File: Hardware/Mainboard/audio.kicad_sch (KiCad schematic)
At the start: 1 part, among them J8 Conn_02x08_Odd_Even

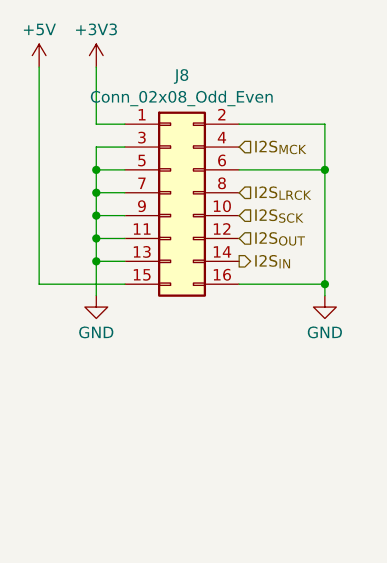
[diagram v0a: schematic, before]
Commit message: Adds more work on the mainboard schematic
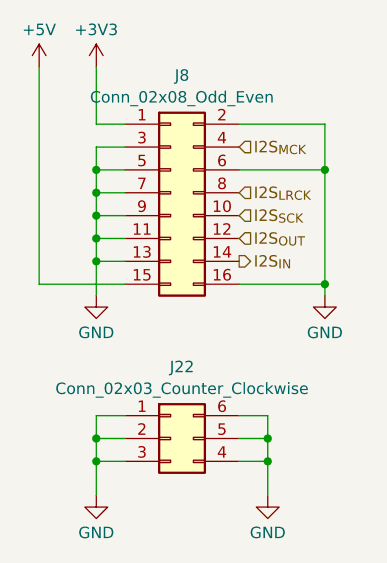
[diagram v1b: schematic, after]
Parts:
- added J22: Conn_02x03_Counter_Clockwise, Connector_PinSocket_2.54mm:PinSocket_2x03_P2.54mm_Vertical, symbol Connector_Generic:Conn_02x03_Counter_Clockwise
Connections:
- net GND: now also J22.1 (Pin_1), J22.2 (Pin_2), J22.3 (Pin_3), J22.4 (Pin_4), J22.5 (Pin_5), J22.6 (Pin_6)
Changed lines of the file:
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@@
   (junction (at 66.675 36.83) (diameter 0) (color 0 0 0 0)
   )
+  (junction (at 41.275 69.215) (diameter 0) (color 0 0 0 0)
+  )
   (junction (at 41.275 46.99) (diameter 0) (color 0 0 0 0)
   )
@@
   (junction (at 41.275 41.91) (diameter 0) (color 0 0 0 0)
   )
+  (junction (at 41.275 66.675) (diameter 0) (color 0 0 0 0)
+  )
   (junction (at 41.275 44.45) (diameter 0) (color 0 0 0 0)
   )
+  (junction (at 60.325 66.675) (diameter 0) (color 0 0 0 0)
+  )
   (junction (at 41.275 39.37) (diameter 0) (color 0 0 0 0)
   )
   (junction (at 66.675 49.53) (diameter 0) (color 0 0 0 0)
   )
+  (junction (at 60.325 69.215) (diameter 0) (color 0 0 0 0)
+  )
   (wire (pts (xy 66.675 36.83) (xy 66.675 49.53))
     (stroke (width 0) (type default))
   )
+  (wire (pts (xy 60.325 66.675) (xy 60.325 69.215))
+    (stroke (width 0) (type default))
+  )
   (wire (pts (xy 41.275 44.45) (xy 41.275 46.99))
     (stroke (width 0) (type default))
@@
     (stroke (width 0) (type default))
   )
+  (wire (pts (xy 41.275 69.215) (xy 41.275 73.025))
+    (stroke (width 0) (type default))
+  )
   (wire (pts (xy 66.675 49.53) (xy 66.675 50.8))
     (stroke (width 0) (type default))
   )
+  (wire (pts (xy 41.275 69.215) (xy 44.45 69.215))
+    (stroke (width 0) (type default))
+  )
+  (wire (pts (xy 60.325 69.215) (xy 60.325 73.025))
+    (stroke (width 0) (type default))
+  )
   (wire (pts (xy 41.275 25.4) (xy 41.275 31.75))
     (stroke (width 0) (type default))
   )
+  (wire (pts (xy 57.15 69.215) (xy 60.325 69.215))
+    (stroke (width 0) (type default))
+  )
+  (wire (pts (xy 44.45 64.135) (xy 41.275 64.135))
+    (stroke (width 0) (type default))
+  )
   (wire (pts (xy 41.275 36.83) (xy 41.275 39.37))
     (stroke (width 0) (type default))
   )
+  (wire (pts (xy 60.325 64.135) (xy 60.325 66.675))
+    (stroke (width 0) (type default))
+  )
+  (wire (pts (xy 41.275 66.675) (xy 41.275 69.215))
+    (stroke (width 0) (type default))
+  )
   (wire (pts (xy 41.275 34.29) (xy 41.275 36.83))
     (stroke (width 0) (type default))
@@
     (stroke (width 0) (type default))
   )
+  (wire (pts (xy 57.15 64.135) (xy 60.325 64.135))
+    (stroke (width 0) (type default))
+  )
   (wire (pts (xy 41.275 39.37) (xy 44.45 39.37))
     (stroke (width 0) (type default))
@@
     (stroke (width 0) (type default))
   )
+  (wire (pts (xy 41.275 64.135) (xy 41.275 66.675))
+    (stroke (width 0) (type default))
+  )
   (wire (pts (xy 57.15 31.75) (xy 66.675 31.75))
     (stroke (width 0) (type default))
@@
     (stroke (width 0) (type default))
   )
+  (wire (pts (xy 41.275 66.675) (xy 44.45 66.675))
+    (stroke (width 0) (type default))
+  )
   (wire (pts (xy 41.275 41.91) (xy 41.275 44.45))
     (stroke (width 0) (type default))
@@
     (stroke (width 0) (type default))
   )
+  (wire (pts (xy 57.15 66.675) (xy 60.325 66.675))
+    (stroke (width 0) (type default))
+  )
   (wire (pts (xy 44.45 49.53) (xy 34.925 49.53))
     (stroke (width 0) (type default))
@@
     (effects (font (size 1.27 1.27)) (justify left))
   )
+  (symbol (lib_id "power:GND") (at 60.325 73.025 0) (unit 1)
+    (in_bom yes) (on_board yes) (dnp no) (fields_autoplaced)
+    (property "Reference" "#PWR0108" (at 60.325 79.375 0)
+      (effects (font (size 1.27 1.27)) hide)
+    )
+    (property "Value" "GND" (at 60.325 77.1581 0)
+      (effects (font (size 1.27 1.27)))
+    )
+    (property "Footprint" "" (at 60.325 73.025 0)
+      (effects (font (size 1.27 1.27)) hide)
+    )
+    (property "Datasheet" "" (at 60.325 73.025 0)
+      (effects (font (size 1.27 1.27)) hide)
+    )
+    (pin "1")
+    (instances
+      (project "Mainboard"
+        (path "/e63e39d7-6ac0-4ffd-8aa3-1841a4541b55/4b5deee2-4545-4875-9d2f-c26357db8f94"
+          (reference "#PWR0108") (unit 1)
+        )
+      )
+    )
+  )
+  (symbol (lib_id "power:GND") (at 41.275 73.025 0) (unit 1)
+    (in_bom yes) (on_board yes) (dnp no) (fields_autoplaced)
+    (property "Reference" "#PWR0107" (at 41.275 79.375 0)
+      (effects (font (size 1.27 1.27)) hide)
+    )
+    (property "Value" "GND" (at 41.275 77.1581 0)
+      (effects (font (size 1.27 1.27)))
+    )
+    (property "Footprint" "" (at 41.275 73.025 0)
+      (effects (font (size 1.27 1.27)) hide)
+    )
+    (property "Datasheet" "" (at 41.275 73.025 0)
+      (effects (font (size 1.27 1.27)) hide)
+    )
+    (pin "1")
+    (instances
+      (project "Mainboard"
+        (path "/e63e39d7-6ac0-4ffd-8aa3-1841a4541b55/4b5deee2-4545-4875-9d2f-c26357db8f94"
+          (reference "#PWR0107") (unit 1)
+        )
+      )
+    )
+  )
   (symbol (lib_id "power:GND") (at 41.275 50.8 0) (unit 1)
     (in_bom yes) (on_board yes) (dnp no) (fields_autoplaced)
@@
         )
       )
+    )
+  )
+  (symbol (lib_id "Connector_Generic:Conn_02x03_Counter_Clockwise") (at 49.53 66.675 0) (unit 1)
+    (in_bom yes) (on_board yes) (dnp no) (fields_autoplaced)
+    (property "Reference" "J22" (at 50.8 58.7207 0)
+      (effects (font (size 1.27 1.27)))
+    )
+    (property "Value" "Conn_02x03_Counter_Clockwise" (at 50.8 61.1449 0)
+      (effects (font (size 1.27 1.27)))
+    )
+    (property "Footprint" "Connector_PinSocket_2.54mm:PinSocket_2x03_P2.54mm_Vertical" (at 49.53 66.675 0)
+      (effects (font (size 1.27 1.27)) hide)
+    )
+    (property "Datasheet" "~" (at 49.53 66.675 0)
+      (effects (font (size 1.27 1.27)) hide)
+    )
+    (pin "2")
+    (pin "5")
+    (pin "3")
+    (pin "1")
+    (pin "4")
+    (pin "6")
+    (instances
+      (project "Mainboard"
+        (path "/e63e39d7-6ac0-4ffd-8aa3-1841a4541b55/4b5deee2-4545-4875-9d2f-c26357db8f94"
+          (reference "J22") (unit 1)
+        )
+      )
